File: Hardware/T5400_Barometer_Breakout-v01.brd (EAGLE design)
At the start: 25.4 x 14 mm, 11 parts, among them U1 T5400

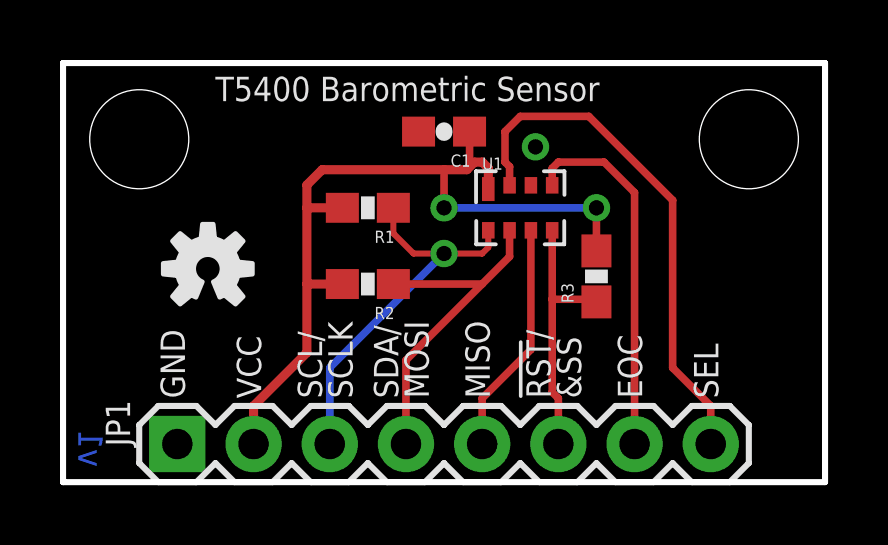
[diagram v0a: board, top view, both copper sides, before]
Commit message: corrected file names to reflect PROTO status made minor modifications to apperance
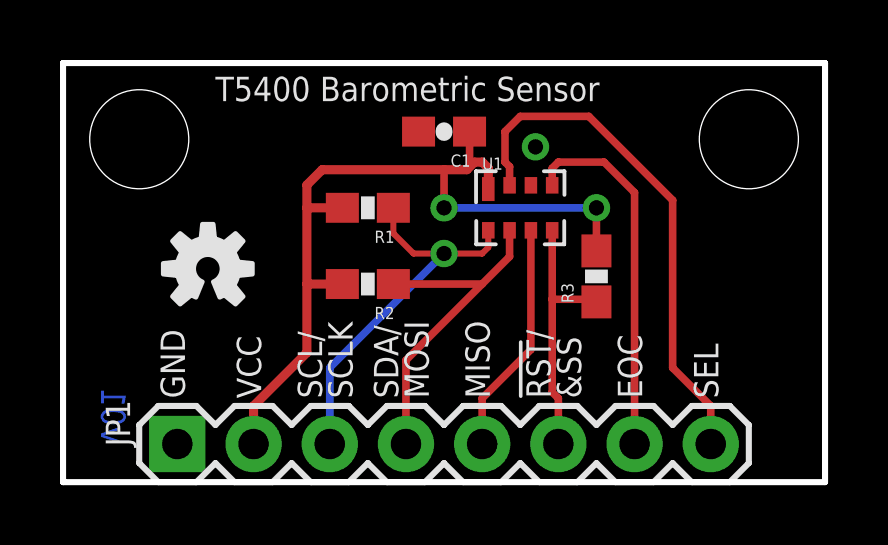
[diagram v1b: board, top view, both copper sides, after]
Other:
- board text added: "v01"
- board text removed: "v1"
